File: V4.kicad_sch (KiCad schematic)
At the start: 31 parts, among them J7 MicroMatch, J8 MicroMatch, U4 TL072, U5 TL072, U6 TL072

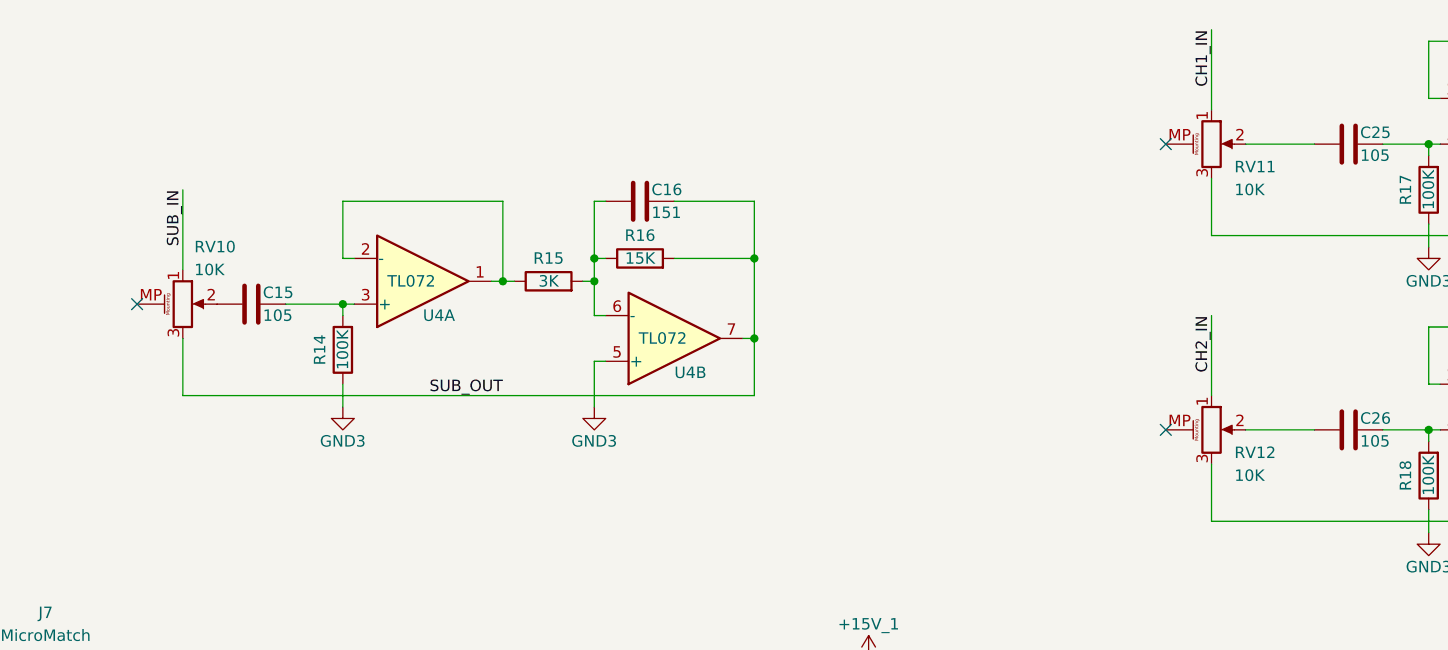
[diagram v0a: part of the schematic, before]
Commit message: Oops, all of the single gang pots were backwards - fixed.
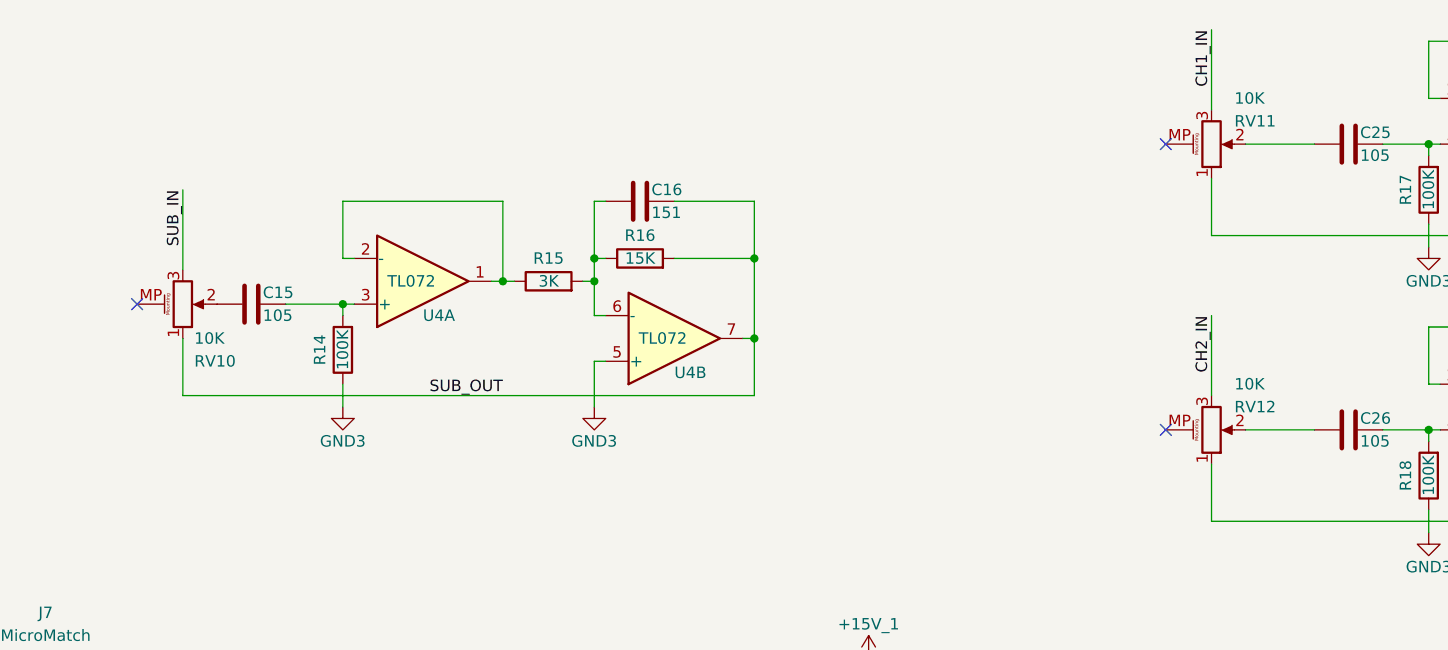
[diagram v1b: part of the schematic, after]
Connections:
- net CH1_IN: now also RV11.3; no longer RV11.1
- net CH1_OUT: now also RV11.1; no longer RV11.3
- net CH2_IN: now also RV12.3; no longer RV12.1
- net CH2_OUT: now also RV12.1; no longer RV12.3
- net SUB_IN: now also RV10.3; no longer RV10.1
- net SUB_OUT: now also RV10.1; no longer RV10.3
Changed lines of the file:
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@@
 		(lib_id "Device:R_Potentiometer_MountingPin")
 		(at 63.5 101.6 0)
+		(mirror x)
 		(unit 1)
 		(exclude_from_sim no)
@@
 		(dnp no)
 		(property "Reference" "RV10"
-			(at 64.77 95.25 0)
+			(at 64.77 107.95 0)
 			(effects
 				(font
@@
 		)
 		(property "Value" "10K"
-			(at 64.77 97.79 0)
+			(at 64.77 105.41 0)
 			(effects
 				(font
@@
 		(lib_id "Device:R_Potentiometer_MountingPin")
 		(at 177.8 83.82 0)
+		(mirror x)
 		(unit 1)
 		(exclude_from_sim no)
@@
 		(dnp no)
 		(property "Reference" "RV11"
-			(at 180.34 86.36 0)
+			(at 180.34 81.28 0)
 			(effects
 				(font
@@
 		)
 		(property "Value" "10K"
-			(at 180.34 88.9 0)
+			(at 180.34 78.74 0)
 			(effects
 				(font
@@
 		(lib_id "Device:R_Potentiometer_MountingPin")
 		(at 177.8 115.57 0)
+		(mirror x)
 		(unit 1)
 		(exclude_from_sim no)
@@
 		(dnp no)
 		(property "Reference" "RV12"
-			(at 180.34 118.11 0)
+			(at 180.34 113.03 0)
 			(effects
 				(font
@@
 		)
 		(property "Value" "10K"
-			(at 180.34 120.65 0)
-			(effects
-				(font
+			(at 180.34 110.49 0)
+			(effects
+				(font

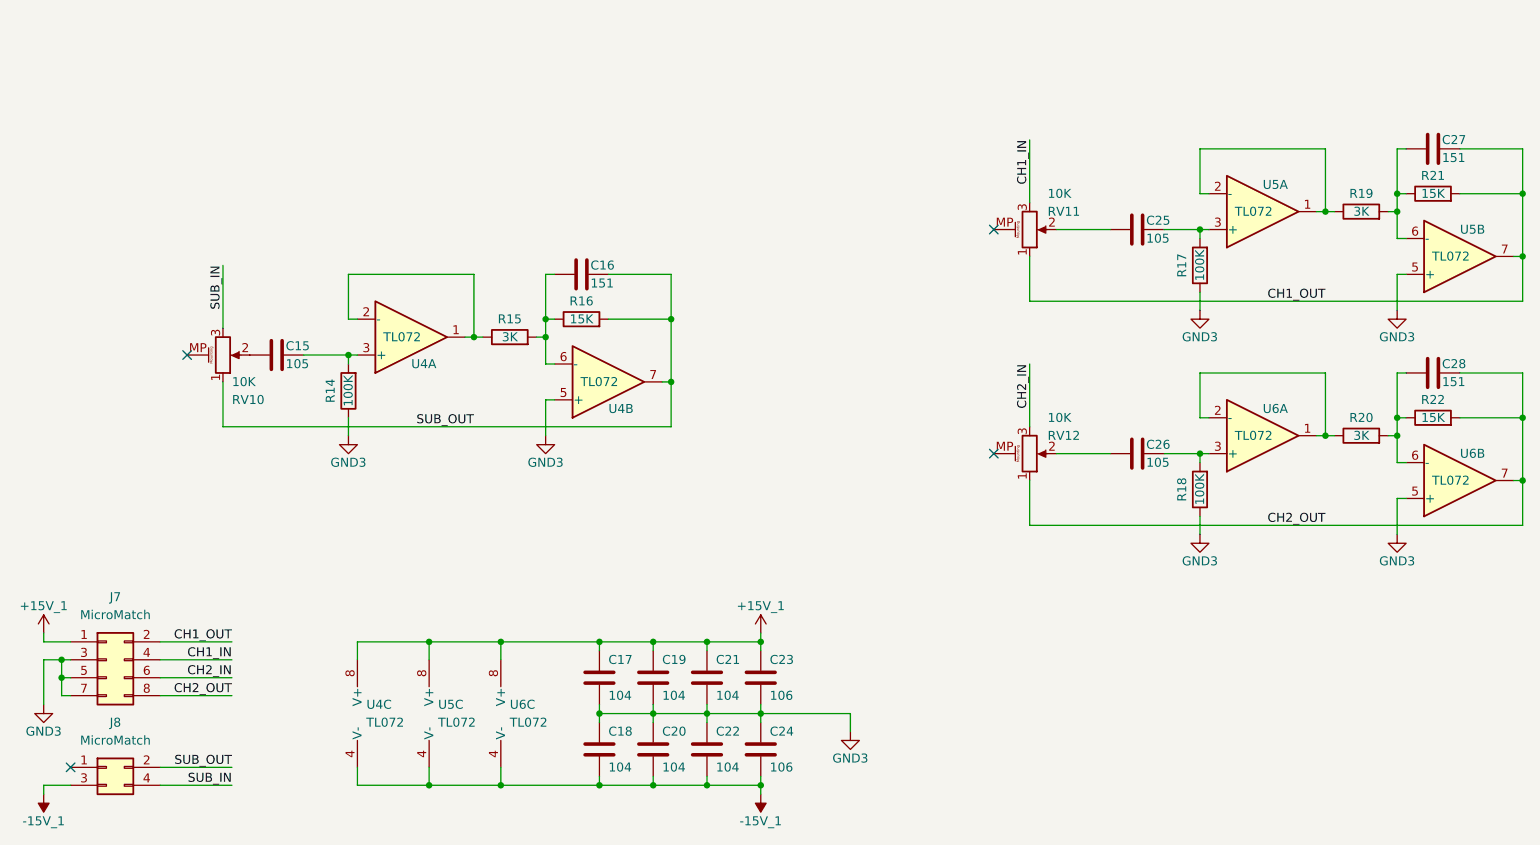
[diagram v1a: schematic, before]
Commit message: Active control topology changed to a single op-amp version.
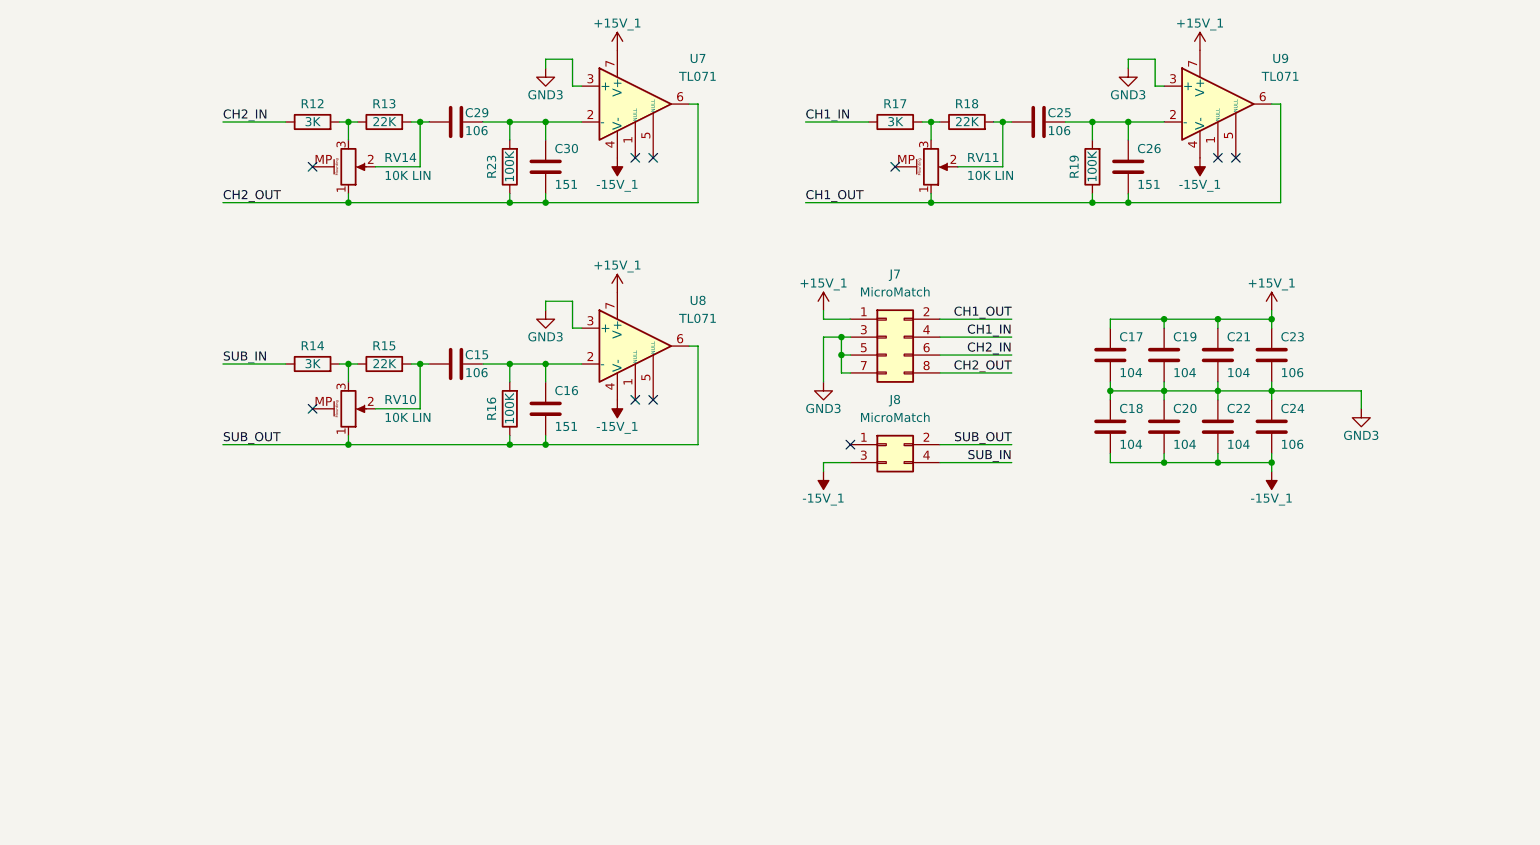
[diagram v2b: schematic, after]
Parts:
- removed C27, C28: 151, Capacitor_SMD:C_0805_2012Metric, symbol Device:C
- removed R20: 3K, Resistor_SMD:R_0805_2012Metric, symbol Device:R
- removed R21, R22: 15K, Resistor_SMD:R_0805_2012Metric, symbol Device:R
- removed RV12: 10K, Potentiometer_THT:Potentiometer_Alps_RK09L_Single_Vertical, symbol Device:R_Potentiometer_MountingPin
- removed U4, U5, U6: TL072, Package_SO:SOIC-8_3.9x4.9mm_P1.27mm, symbol Amplifier_Operational:TL072
- added C29: 106, Capacitor_SMD:C_1210_3225Metric, symbol Device:C
- added C30: 151, Capacitor_SMD:C_0805_2012Metric, symbol Device:C
- added R12: 3K, Resistor_SMD:R_0805_2012Metric, symbol Device:R
- added R13: 22K, Resistor_SMD:R_0805_2012Metric, symbol Device:R
- added R23: 100K, Resistor_SMD:R_0805_2012Metric, symbol Device:R
- added RV14: 10K LIN, Potentiometer_THT:Potentiometer_Alps_RK09L_Single_Vertical, symbol Device:R_Potentiometer_MountingPin
- added U7, U8, U9: TL071, Package_SO:SOIC-8_3.9x4.9mm_P1.27mm, symbol Amplifier_Operational:TL071
- C15, C25: value 105 -> 106
- C26: value 105 -> 151; footprint Capacitor_SMD:C_1210_3225Metric -> Capacitor_SMD:C_0805_2012Metric
- R14, R17: value 100K -> 3K
- R15: value 3K -> 22K
- R16: value 15K -> 100K
- R18: value 100K -> 22K
- R19: value 3K -> 100K
- RV10, RV11: value 10K -> 10K LIN
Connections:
- net +15V_1: now also U7.7 (V+), U8.7 (V+), U9.7 (V+)
- net -15V_1: now also U7.4 (V-), U8.4 (V-), U9.4 (V-)
- net CH1_IN: now also R17.1; no longer RV11.3
- net CH1_OUT: now also C26.2, R19.1, U9.6
- net CH2_IN: now also R12.1
- net CH2_OUT: now also C30.2, R23.1, RV14.1, U7.6
- net GND3: now also U7.3 (+), U8.3 (+), U9.3 (+); no longer R14.1, R17.1, R18.1
- net SUB_IN: now also R14.1; no longer RV10.3
- net SUB_OUT: now also R16.1, U8.6; no longer R16.2
- net at C25.2: now also C26.1, R19.2, U9.2 (-); no longer R17.2
- net at R15.1: now also R14.2, RV10.3
- net at C25.1, RV11.2: now also R18.2
- net at C15.1, RV10.2: now also R15.2
- net at C15.2: now also C16.1, R16.2, U8.2 (-); no longer R14.2
- new net: C29.1, R13.2, RV14.2
- new net: C29.2, C30.1, R23.2, U7.2 (-)
- new net: R17.2, R18.1, RV11.3
- new net: R12.2, R13.1, RV14.3
- no-connect marks 4 -> 10
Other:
- moved on the sheet: C17, C18, C19, C20, C21, C22, C23, C24, J7, J8
